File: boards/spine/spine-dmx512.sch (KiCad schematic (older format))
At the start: 20 parts, among them CON6 XLR-3 Female, Q1 DMN3190LDW, T1 10/100baseT transformer, U3 AP2204K-5.0, U5 NC7WZ14, U6 ST485E

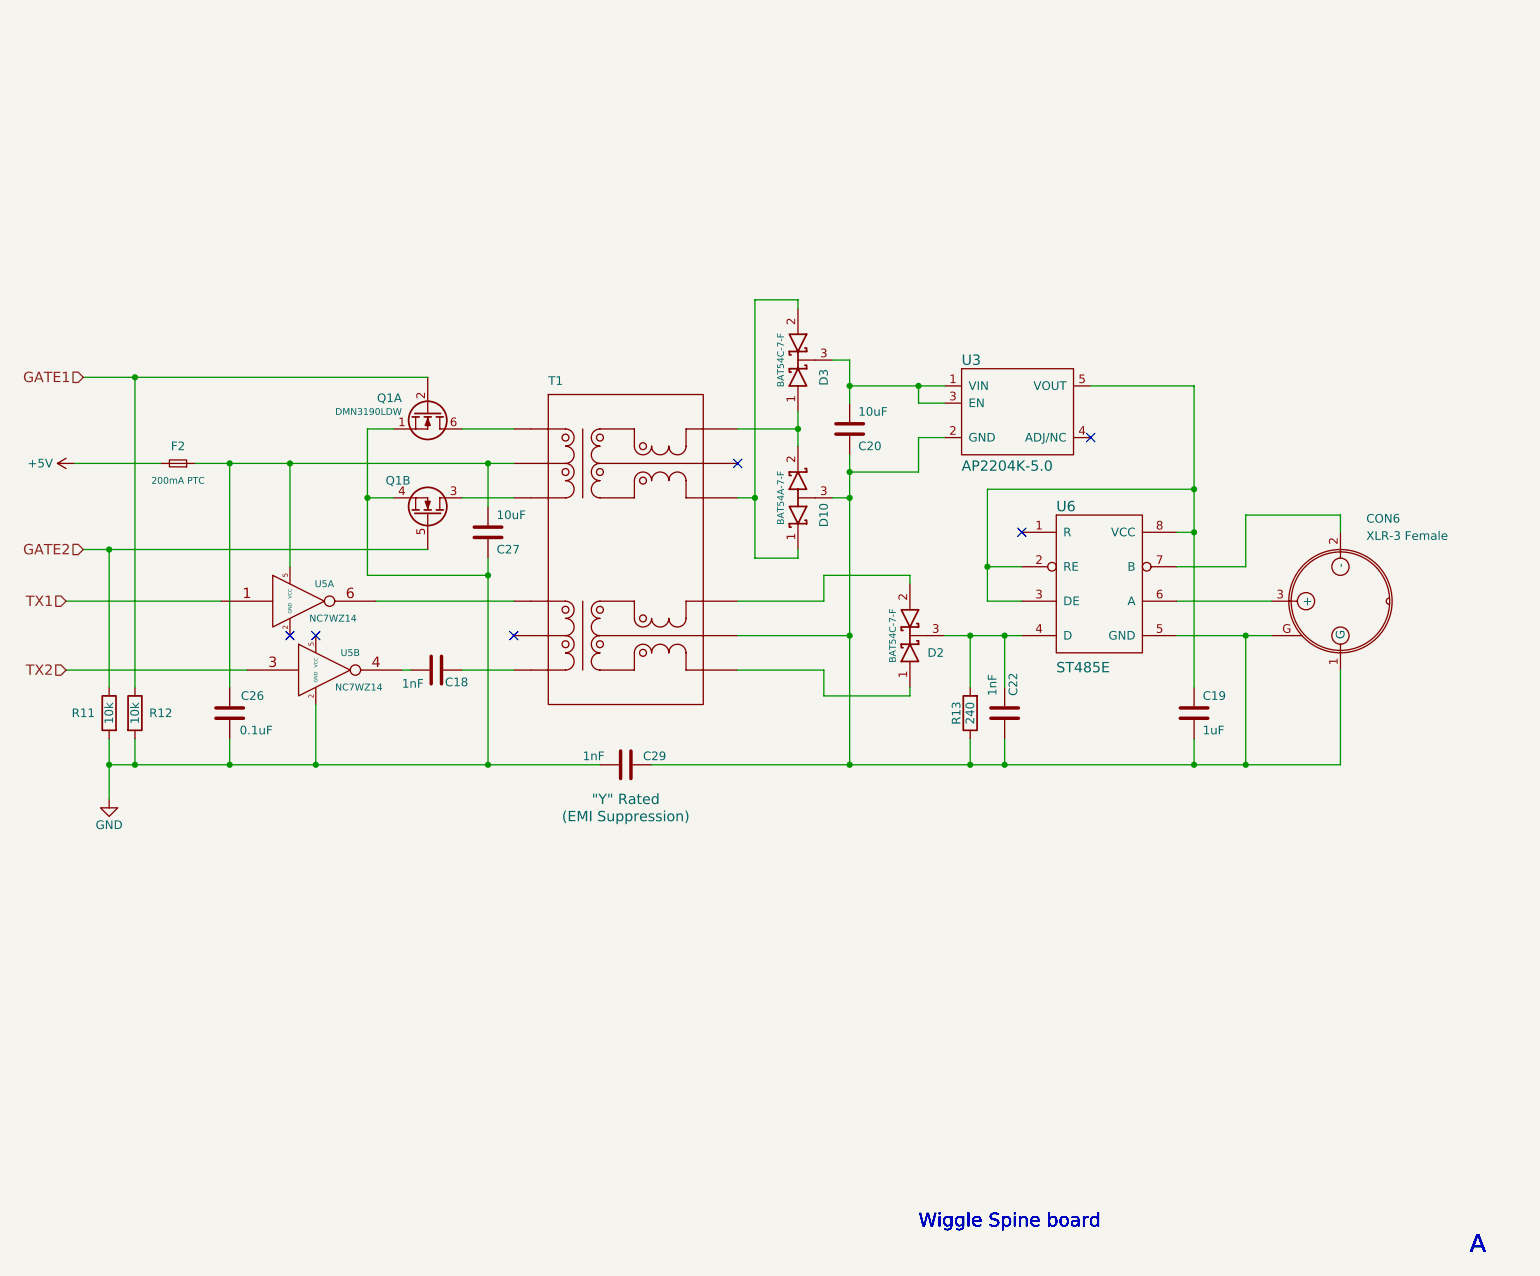
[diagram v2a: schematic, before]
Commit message: BOM tweaks, starting DC/DC fixes
VCC is not active until EN goes high, so EN must be
connected to VIN via the 100k resistor. Internal resistance
is 5k to a 3V zener.
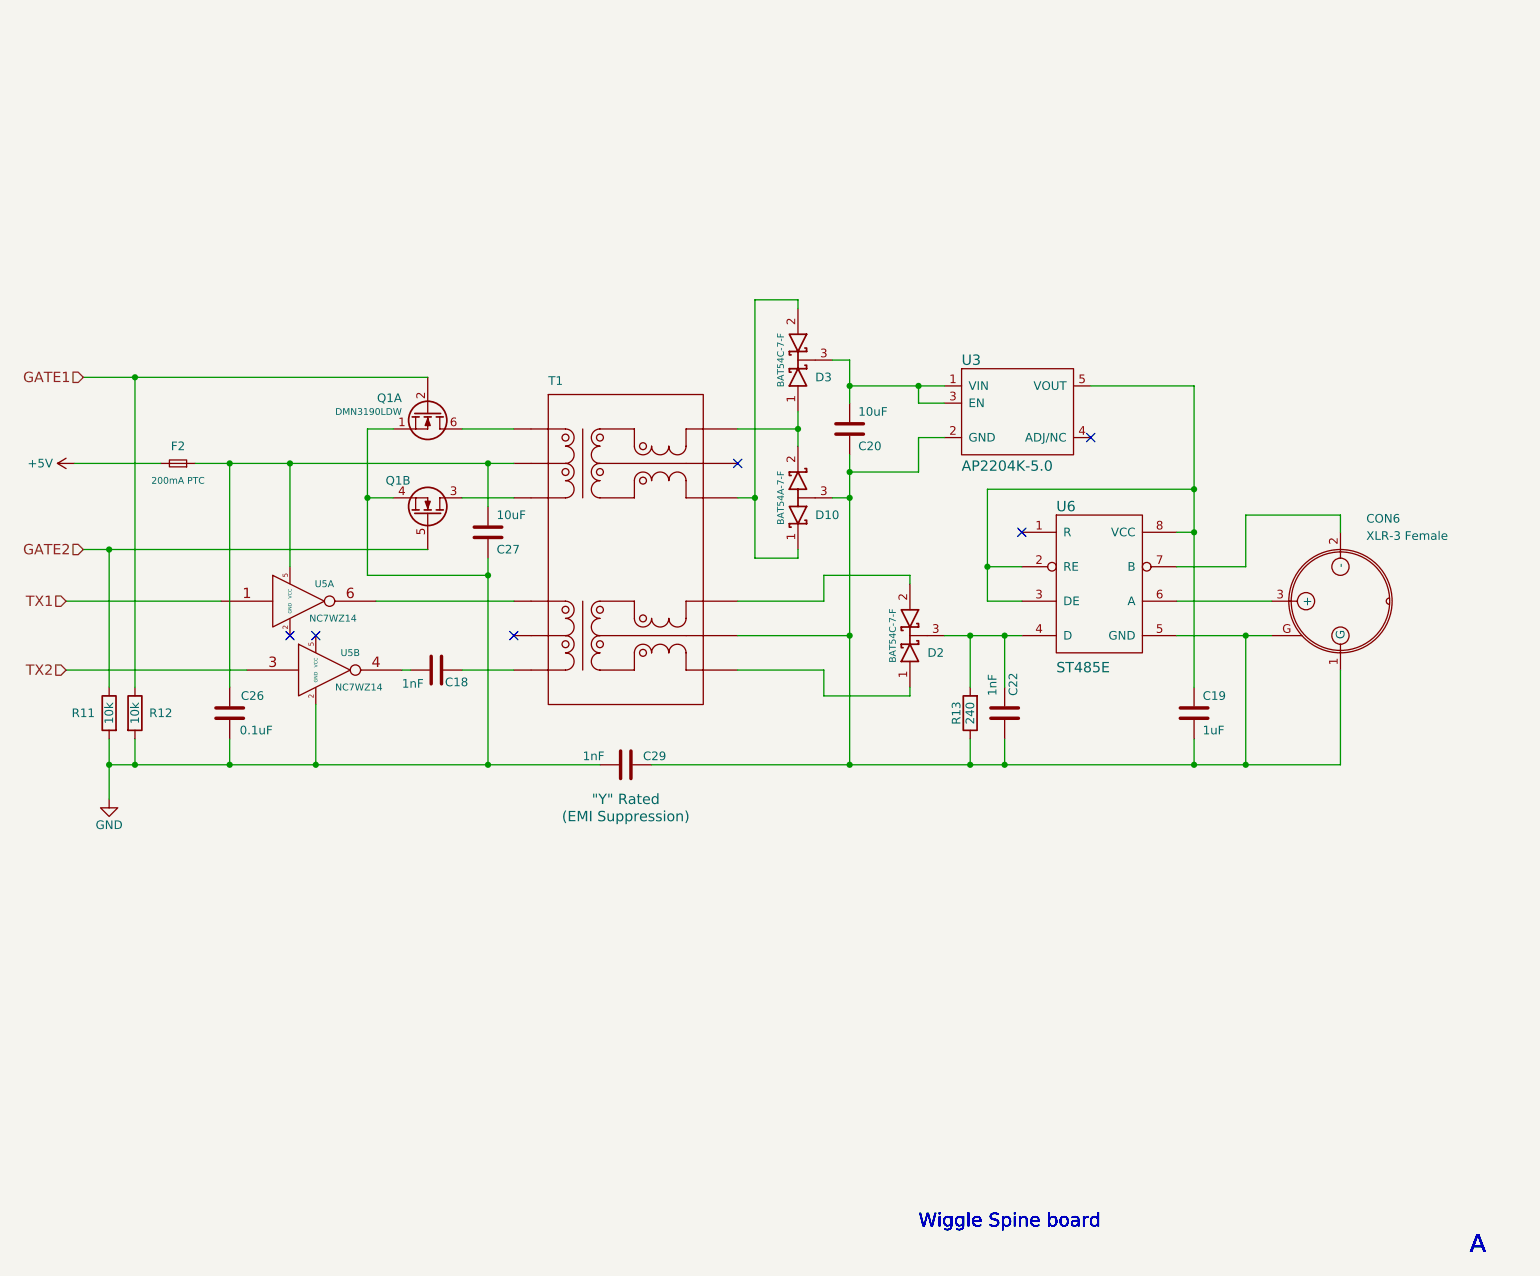
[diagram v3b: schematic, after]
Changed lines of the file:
@@
 U 1 1 563EE535
 P 6000 2700
-F 0 "D3" H 5900 2550 50  0000 C CNN
+F 0 "D3" V 5900 2600 50  0000 R CNN
 F 1 "BAT54 2x common cathode" H 6000 2800 50  0001 C CNN
 F 2 "TO_SOT_Packages_SMD:SOT-23" H 6000 2700 60  0001 C CNN
@@
 72 0F 1C A9 DC 70 49 CB 79 33 88 85 99 AD 01 6C 4B 10 FC 3B 13 DE 3B 37 68 79 AD 07 BC 00 3C 0E
 3C 31 EE E3 D8 E7 0F 03 D7 7B 9F FB C1 E1 FF 01 18 C4 96 1D B8 0E 40 07 00 00 00 00 49 45 4E 44
-AE 42 60 82 FF
+AE 42 60 82 00
 EndData
 $EndBitmap
@@
 72 0F 1C A9 DC 70 49 CB 79 33 88 85 99 AD 01 6C 4B 10 FC 3B 13 DE 3B 37 68 79 AD 07 BC 00 3C 0E
 3C 31 EE E3 D8 E7 0F 03 D7 7B 9F FB C1 E1 FF 01 18 C4 96 1D B8 0E 40 07 00 00 00 00 49 45 4E 44
-AE 42 60 82 FF
+AE 42 60 82 00
 EndData
 $EndBitmap
@@
 U 1 1 56768910
 P 6000 3500
-F 0 "D10" H 5900 3350 50  0000 C CNN
+F 0 "D10" V 5900 3400 50  0000 R CNN
 F 1 "BAT54 2x common anode" H 6000 3600 50  0001 C CNN
 F 2 "TO_SOT_Packages_SMD:SOT-23" H 6000 3500 60  0001 C CNN
@@
 72 0F 1C A9 DC 70 49 CB 79 33 88 85 99 AD 01 6C 4B 10 FC 3B 13 DE 3B 37 68 79 AD 07 BC 00 3C 0E
 3C 31 EE E3 D8 E7 0F 03 D7 7B 9F FB C1 E1 FF 01 18 C4 96 1D B8 0E 40 07 00 00 00 00 49 45 4E 44
-AE 42 60 82 00
+AE 42 60 82 FF
 EndData
 $EndBitmap
@@
 $EndComp
 Wire Wire Line
-	5150 5050 6300 5050
-Wire Wire Line
-	6300 5050 7000 5050
-Wire Wire Line
-	7000 5050 7200 5050
-Wire Wire Line
-	7200 5050 8300 5050
-Wire Wire Line
-	8300 5050 8600 5050
-Wire Wire Line
-	8600 5050 9150 5050
+	5150 5050 9150 5050
 Wire Wire Line
 	9150 5050 9150 4500
 Wire Wire Line
-	6850 4300 7000 4300
-Wire Wire Line
-	7000 4300 7200 4300
-Wire Wire Line
-	7200 4300 7300 4300
+	6850 4300 7300 4300
 Connection ~ 7000 4300
 Wire Wire Line
@@
 	7100 3900 7300 3900
 Wire Wire Line
-	8200 4300 8600 4300
-Wire Wire Line
-	8600 4300 8750 4300
+	8200 4300 8750 4300
 Wire Wire Line
 	8600 4300 8600 5050
 Wire Wire Line
-	6000 3000 6000 3100
-Wire Wire Line
-	6000 3100 6000 3200
+	6000 3000 6000 3200
 Wire Wire Line
 	5650 3100 6000 3100
@@
 	6000 3850 5750 3850
 Wire Wire Line
-	5750 3850 5750 3500
-Wire Wire Line
-	5750 3500 5750 2350
+	5750 3850 5750 2350
 Wire Wire Line
 	5750 3500 5650 3500
@@
 	6200 2700 6300 2700
 Wire Wire Line
-	6300 2700 6300 2850
-Wire Wire Line
-	6300 2850 6300 2950
-Wire Wire Line
-	6300 3250 6300 3350
+	6300 2700 6300 2950
 Wire Wire Line
-	6300 3350 6300 3500
-Wire Wire Line
-	6300 3500 6300 4300
-Wire Wire Line
-	6300 4300 6300 5050
+	6300 3250 6300 5050
 Wire Wire Line
 	6300 3500 6200 3500
@@
 	6700 2950 6850 2950
 Wire Wire Line
-	6300 2850 6700 2850
-Wire Wire Line
-	6700 2850 6850 2850
+	6300 2850 6850 2850
 Wire Wire Line
 	6700 2850 6700 2950
@@
 	7700 2850 8300 2850
 Wire Wire Line
-	8300 2850 8300 3450
-Wire Wire Line
-	8300 3450 8300 3700
-Wire Wire Line
-	8300 3700 8300 4600
+	8300 2850 8300 4600
 Connection ~ 8600 5050
 Connection ~ 6300 5050
@@
 Connection ~ 7200 5050
 Wire Wire Line
-	7100 3450 7100 3900
-Wire Wire Line
-	7100 3900 7100 4100
+	7100 3450 7100 4100
 Wire Wire Line
 	8300 3450 7100 3450
@@
 Connection ~ 8300 3450
 Wire Wire Line
-	2000 5050 2150 5050
-Wire Wire Line
-	2150 5050 2700 5050
-Wire Wire Line
-	2700 5050 3200 5050
-Wire Wire Line
-	3200 5050 4200 5050
-Wire Wire Line
-	4200 5050 4850 5050
+	2000 5050 4850 5050
 Wire Wire Line
 	1750 4500 2800 4500
@@
 Connection ~ 3200 5050
 Wire Wire Line
-	2500 3300 2700 3300
-Wire Wire Line
-	2700 3300 3050 3300
-Wire Wire Line
-	3050 3300 4200 3300
-Wire Wire Line
-	4200 3300 4350 3300
+	2500 3300 4350 3300
 Wire Wire Line
 	4200 3300 4200 3550
 Wire Wire Line
-	4200 3850 4200 3950
-Wire Wire Line
-	4200 3950 4200 5050
+	4200 3850 4200 5050
 Connection ~ 4200 5050
 Wire Wire Line
@@
 	3500 3950 4200 3950
 Wire Wire Line
-	3500 3100 3500 3500
-Wire Wire Line
-	3500 3500 3500 3950
+	3500 3100 3500 3950
 Wire Wire Line
 	3500 3100 3650 3100
@@
 Connection ~ 3500 3500
 Wire Wire Line
-	1850 3800 2000 3800
-Wire Wire Line
-	2000 3800 3850 3800
+	1850 3800 3850 3800
 Wire Wire Line
-	1850 2800 2150 2800
-Wire Wire Line
-	2150 2800 3850 2800
+	1850 2800 3850 2800
 Wire Wire Line
 	2000 4600 2000 3800
@@
 	2150 4600 2150 2800
 Wire Wire Line
-	2000 4900 2000 5050
-Wire Wire Line
-	2000 5050 2000 5250
+	2000 4900 2000 5250
 Connection ~ 2700 5050
 Wire Wire Line

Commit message: BOM cleanup
Especially fix the confusing and mostly incorrect Mfg/Mfr stuff that I inherited from somewhere.
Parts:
- C18, C22: Mfg1 (none) -> Murata; Mfg1Id (none) -> GRM216R71H102KA01D; MfgId GRM216R71H102KA01D -> (none); MfrId Murata -> (none)
- C19: Mfg1 (none) -> Murata; Mfg1Id (none) -> GRM219R61H105KA73D; MfgId GRM219R61H105KA73D -> (none); MfrId Murata -> (none)
- C20, C27: Mfg1 (none) -> Murata; Mfg1Id (none) -> GRM31CR61H106MA12L; MfgId GRM31CR61H106MA12L -> (none); MfrId Murata -> (none)
- C26: Mfg1 (none) -> Murata; Mfg1Id (none) -> GRM21BR71H104MA01L; MfgId GRM21BR71H104MA01L -> (none); MfrId Murata -> (none)
- C29: Mfg1 (none) -> EPCOS (TDK); Mfg1Id (none) -> B32021A3102M189; MfgId B32021A3102M189 -> (none); MfrId EPCOS (TDK) -> (none)
- CON6: Mfg1 (none) -> Neutrik; Mfg1Id (none) -> NC3FAAH2-0; MfgId NC3FAAH2-0 -> (none); MfrId Neutrik -> (none)
- D10: Mfg1 (none) -> Diodes Inc; Mfg1Id (none) -> BAT54A-7-F; MfgId BAT54A-7-F -> (none); MfrId Diodes Inc -> (none)
- D2, D3: Mfg1 (none) -> Diodes Inc; Mfg1Id (none) -> BAT54C-7-F; MfgId BAT54C-7-F -> (none); MfrId Diodes Inc -> (none)
- F2: Mfg1 (none) -> Bel Fuse; Mfg1Id (none) -> 0ZCJ0020FF2E; MfgId 0ZCJ0020FF2E -> (none); MfrId Bel Fuse -> (none)
- Q1: Mfg1 (none) -> Diodes Inc; Mfg1Id (none) -> DMN3190LDW-7; MfgId Diodes Inc -> (none); MfrId DMN3190LDW-7 -> (none)
- Q1: Mfg1 (none) -> DMN3190LDW-7; Mfg1Id (none) -> Diodes Inc; MfgId Diodes Inc -> (none); MfrId DMN3190LDW-7 -> (none)
- R11, R12: Mfg1 (none) -> Stackpole; Mfg1Id (none) -> RMCF0805JT10K0; MfgId RMCF0805JT10K0 -> (none); MfrId Stackpole -> (none)
- R13: Mfg1 (none) -> Stackpole; Mfg1Id (none) -> RMCF0805JT240R; MfgId RMCF0805JT240R -> (none); MfrId Stackpole -> (none)
- T1: Mfg1 (none) -> Bourns; Mfg1Id (none) -> PT61018PEL; MfgId PT61018PEL -> (none); MfrId Bourns -> (none)
- U3: Mfg1 (none) -> Diodes Inc; Mfg1Id (none) -> AP2204K-5.0TRG1; MfgId AP2204K-5.0TRG1 -> (none); MfrId Diodes Inc -> (none)
- U5: Mfg1 (none) -> Fairchild; Mfg1Id (none) -> NC7WZ14P6X; MfgId NC7WZ14P6X -> (none); MfrId Fairchild -> (none)
- U6: Mfg1 (none) -> STMicroelectronics; Mfg1Id (none) -> ST485ECDR; MfgId ST485ECDR -> (none); MfrId STMicroelectronics -> (none)
